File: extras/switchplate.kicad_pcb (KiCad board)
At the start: 2 copper layers, 344.4 x 121.3 mm, 2 parts

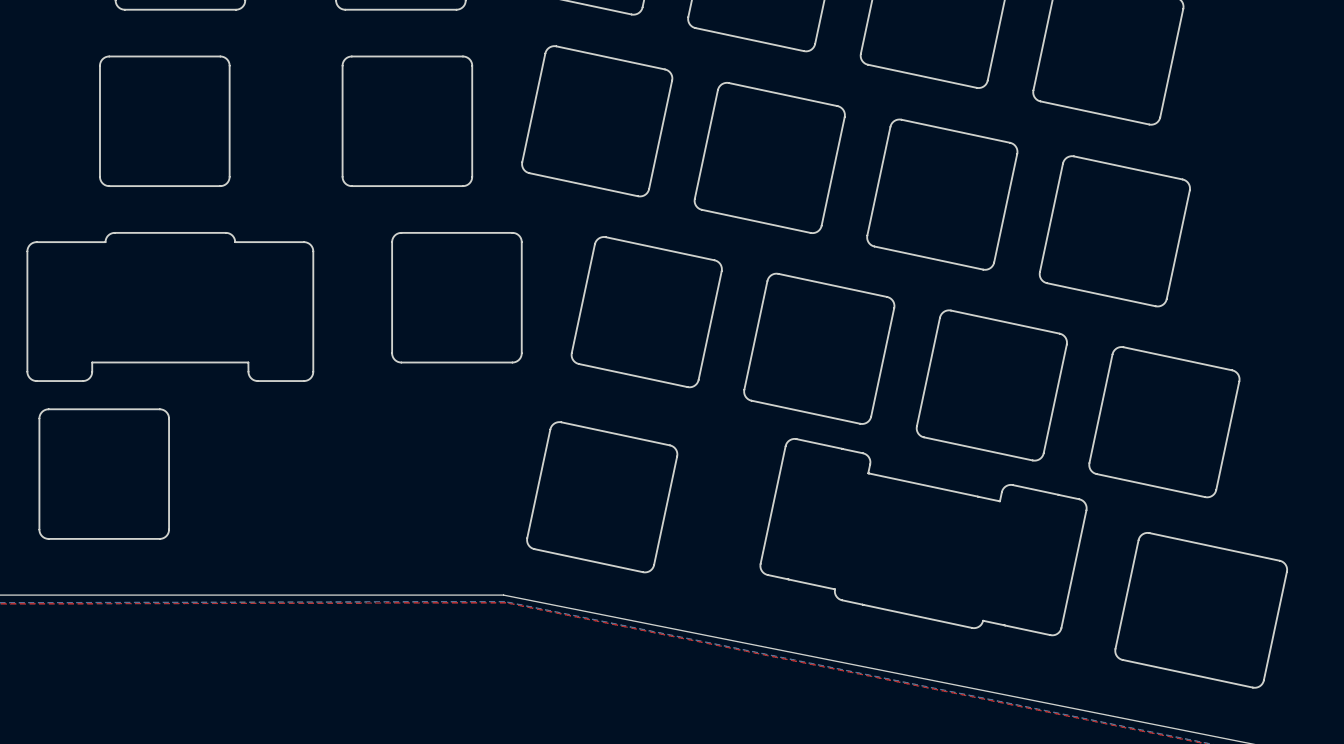
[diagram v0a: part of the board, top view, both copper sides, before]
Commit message: update plate and add feet to bottom
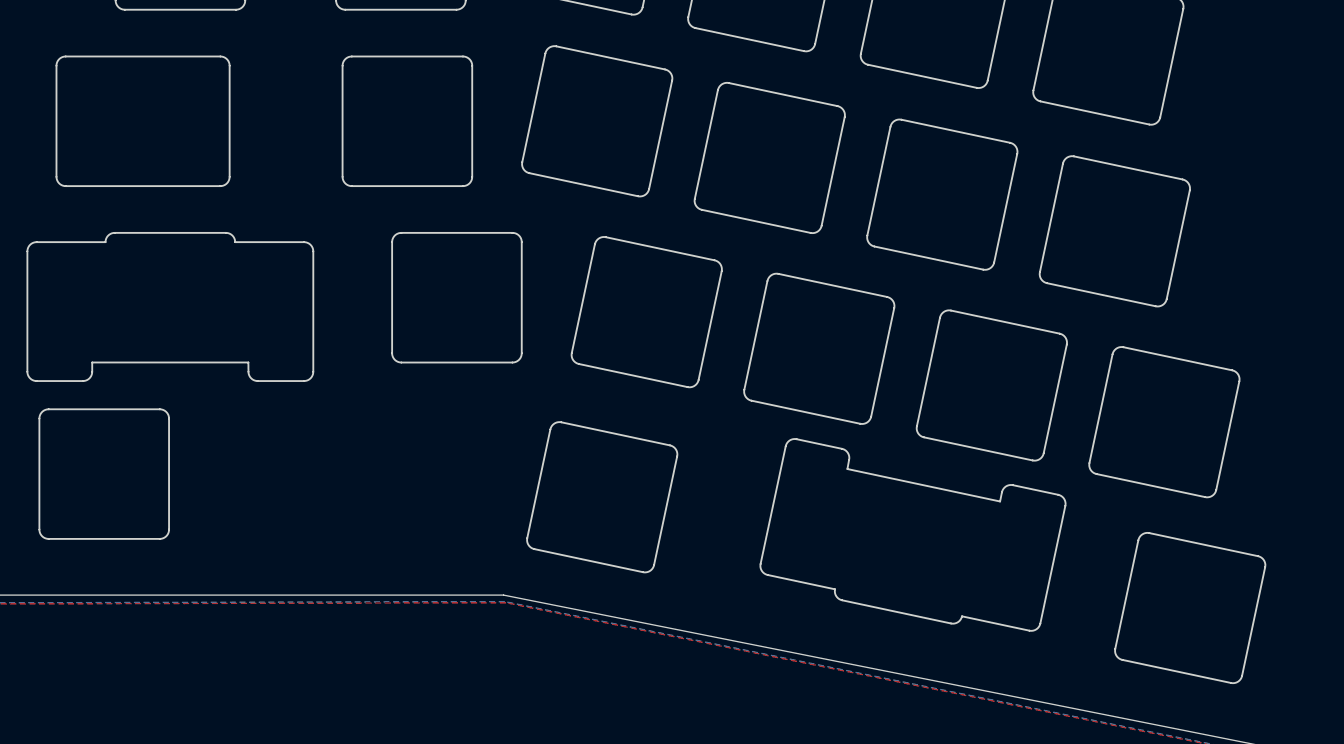
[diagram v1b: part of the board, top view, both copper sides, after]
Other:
- outline, holes or cut-outs redrawn
